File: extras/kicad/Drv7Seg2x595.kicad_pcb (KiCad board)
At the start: 2 copper layers, 67.4 x 50.8 mm, 33 parts, among them IC1 74HC595, IC2 74HC595, J1 INTERFACE, J2 PWR_LED_JMP, Q1 MMBT3904, Q2 MMBT3904, Q3 MMBT3904, Q4 MMBT3904

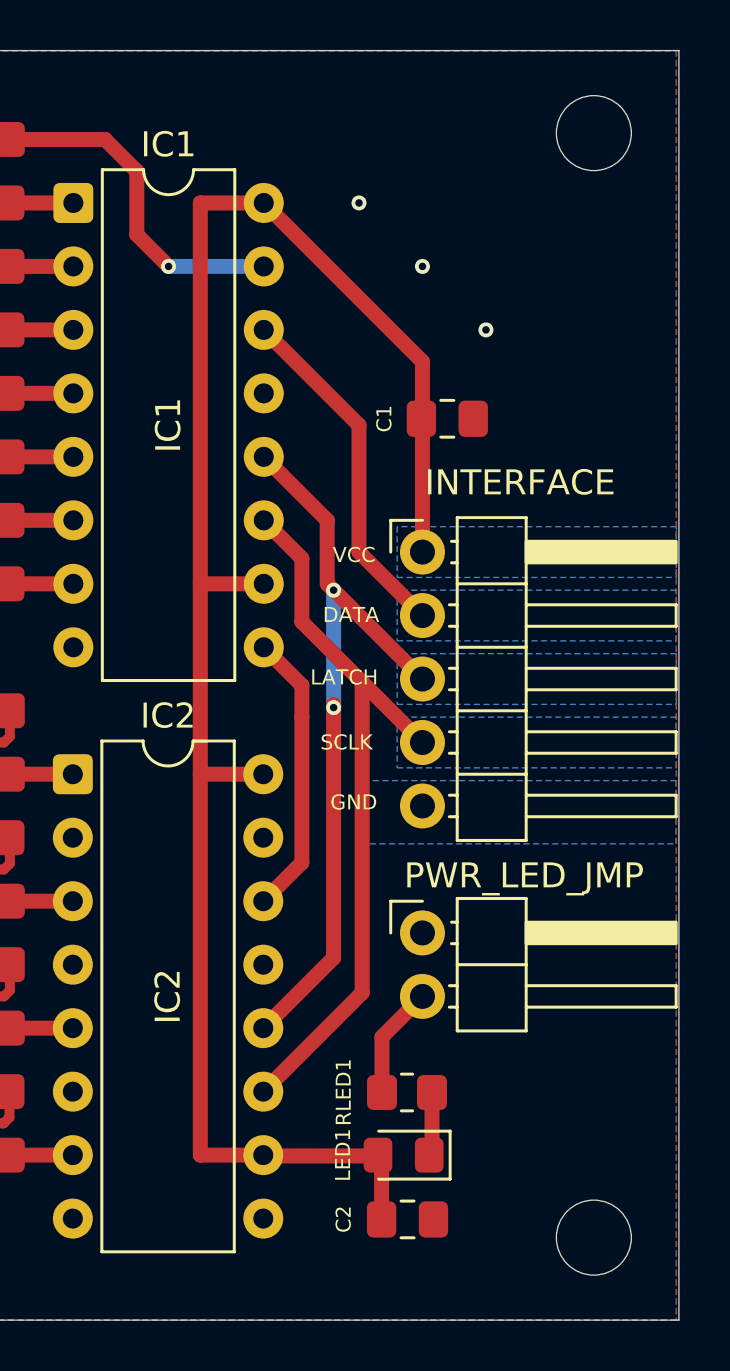
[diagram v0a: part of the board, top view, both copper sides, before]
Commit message: Move SMD caps, power indicator LED and its resistor behind the headers' line.
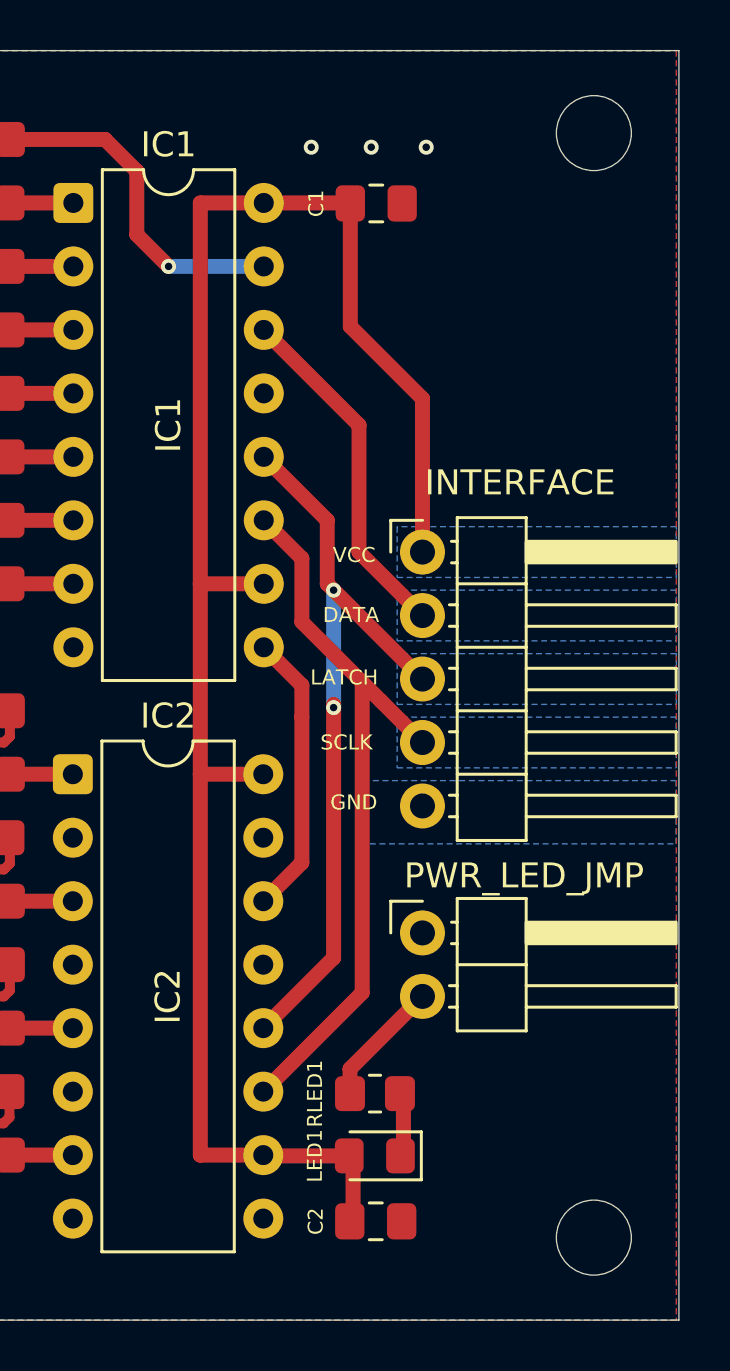
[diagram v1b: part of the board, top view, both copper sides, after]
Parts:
- moved C1 9.07 mm to (172.1, 73.7)
- moved RLED1 1.28 mm to (172.1, 109.3)
- moved C2 1.27 mm to (172.1, 114.4)
- moved D1 1.15 mm to (172.1, 111.8)
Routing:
- net VCC: track 72.1 -> 72.9 mm
- net Net-(J2-Pin_1): track 4.55 -> 5.11 mm
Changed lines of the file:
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@@
 	(footprint "Capacitor_SMD:C_0805_2012Metric_Pad1.18x1.45mm_HandSolder"
 		(layer "F.Cu")
-		(at 173.3925 114.334 180)
+		(at 172.12 114.41 180)
 		(descr "Capacitor SMD 0805 (2012 Metric), square (rectangular) end terminal, IPC-7351 nominal with elongated pad for handsoldering. (Body size source: IPC-SM-782 page 76, https://www.pcb-3d.com/wordpress/wp-content/uploads/ipc-sm-782a_amendment_1_and_2.pdf, https://docs.google.com/spreadsheets/d/1BsfQQcO9C6DZCsRaXUlFlo91Tg2WpOkGARC1WS5S8t0/edit?usp=sharing), generated with kicad-footprint-generator")
 		(tags "capacitor handsolder")
 		(property "Reference" "C2"
-			(at 2.5521 0.0086 90)
+			(at 2.4 0 90)
 			(layer "F.SilkS")
 			(effects
@@
 	(footprint "Resistor_SMD:R_0805_2012Metric_Pad1.20x1.40mm_HandSolder"
 		(layer "F.Cu")
-		(at 173.371 109.254)
+		(at 172.09 109.3)
 		(descr "Resistor SMD 0805 (2012 Metric), square (rectangular) end terminal, IPC-7351 nominal with elongated pad for handsoldering. (Body size source: IPC-SM-782 page 72, https://www.pcb-3d.com/wordpress/wp-content/uploads/ipc-sm-782a_amendment_1_and_2.pdf), generated with kicad-footprint-generator")
 		(tags "resistor handsolder")
 		(property "Reference" "RLED1"
-			(at -2.5306 -0.0086 90)
+			(at -2.4 0 90)
 			(layer "F.SilkS")
 			(effects
@@
 	(footprint "LED_SMD:LED_0805_2012Metric_Pad1.15x1.40mm_HandSolder"
 		(layer "F.Cu")
-		(at 173.237 111.76 180)
+		(at 172.085 111.79 180)
 		(descr "LED SMD 0805 (2012 Metric), square (rectangular) end terminal, IPC-7351 nominal, (Body size source: https://docs.google.com/spreadsheets/d/1BsfQQcO9C6DZCsRaXUlFlo91Tg2WpOkGARC1WS5S8t0/edit?usp=sharing), generated with kicad-footprint-generator")
 		(tags "LED handsolder")
@@
 		)
 		(property "Value" "LED1"
-			(at 2.422 0 90)
+			(at 2.4 0 90)
 			(layer "F.SilkS")
 			(effects
@@
 	(footprint "Capacitor_SMD:C_0805_2012Metric_Pad1.18x1.45mm_HandSolder"
 		(layer "F.Cu")
-		(at 174.9845 82.296)
+		(at 172.14 73.68)
 		(descr "Capacitor SMD 0805 (2012 Metric), square (rectangular) end terminal, IPC-7351 nominal with elongated pad for handsoldering. (Body size source: IPC-SM-782 page 76, https://www.pcb-3d.com/wordpress/wp-content/uploads/ipc-sm-782a_amendment_1_and_2.pdf, https://docs.google.com/spreadsheets/d/1BsfQQcO9C6DZCsRaXUlFlo91Tg2WpOkGARC1WS5S8t0/edit?usp=sharing), generated with kicad-footprint-generator")
 		(tags "capacitor handsolder")
 		(property "Reference" "C1"
-			(at -2.5185 0 90)
+			(at -2.4 0 90)
 			(layer "F.SilkS")
 			(effects
@@
 	)
 	(segment
-		(start 167.654 111.794)
-		(end 167.62 111.76)
+		(start 167.64 73.66)
+		(end 171.0825 73.66)
 		(width 0.6)
 		(layer "F.Cu")
@@
 	)
 	(segment
-		(start 172.355 111.794)
-		(end 172.355 114.334)
+		(start 167.654 111.794)
+		(end 167.62 111.76)
 		(width 0.6)
 		(layer "F.Cu")
@@
 	)
 	(segment
-		(start 173.99 87.63)
-		(end 173.99 80.01)
+		(start 171.213 111.824)
+		(end 171.213 114.364)
 		(width 0.6)
 		(layer "F.Cu")
@@
 	)
 	(segment
-		(start 165.1 88.9)
-		(end 165.1 73.66)
+		(start 171.0825 73.66)
+		(end 171.1025 73.68)
 		(width 0.6)
 		(layer "F.Cu")
@@
 	)
 	(segment
-		(start 172.355 111.794)
-		(end 167.654 111.794)
+		(start 165.1 88.9)
+		(end 165.1 73.66)
 		(width 0.6)
 		(layer "F.Cu")
@@
 	)
 	(segment
-		(start 165.1 73.66)
-		(end 167.64 73.66)
+		(start 171.1025 78.6025)
+		(end 173.99 81.49)
 		(width 0.6)
 		(layer "F.Cu")
@@
 	)
 	(segment
-		(start 173.99 80.01)
+		(start 165.1 73.66)
 		(end 167.64 73.66)
 		(width 0.6)
@@
 	)
 	(segment
+		(start 173.947 87.587)
+		(end 173.99 87.63)
+		(width 0.6)
+		(layer "F.Cu")
+		(net 9)
+	)
+	(segment
 		(start 165.1 96.52)
 		(end 165.1 111.76)
@@
 	)
 	(segment
+		(start 171.06 111.79)
+		(end 167.65 111.79)
+		(width 0.6)
+		(layer "F.Cu")
+		(net 9)
+	)
+	(segment
+		(start 171.1025 73.68)
+		(end 171.1025 78.6025)
+		(width 0.6)
+		(layer "F.Cu")
+		(net 9)
+	)
+	(segment
 		(start 167.64 88.9)
 		(end 165.1 88.9)
@@
 		(net 9)
 	)
+	(segment
+		(start 173.99 81.49)
+		(end 173.99 87.63)
+		(width 0.6)
+		(layer "F.Cu")
+		(net 9)
+	)
+	(segment
+		(start 167.65 111.79)
+		(end 167.62 111.76)
+		(width 0.2)
+		(layer "F.Cu")
+		(net 9)
+	)
 	(via
 		(at 153.67 103.886)
@@
 	)
 	(via
-		(at 148.59 72.39)
+		(at 174.14 71.43)
 		(size 0.6)
 		(drill 0.3)
@@
 	)
 	(via
-		(at 173.99 76.2)
+		(at 148.59 72.39)
 		(size 0.6)
 		(drill 0.3)
@@
 	)
 	(via
-		(at 171.45 73.66)
+		(at 171.94 71.43)
 		(size 0.6)
 		(drill 0.3)
@@
 	)
 	(via
-		(at 176.53 78.74)
+		(at 156.337 114.3)
 		(size 0.6)
 		(drill 0.3)
@@
 	)
 	(via
-		(at 156.337 114.3)
+		(at 148.59 74.93)
 		(size 0.6)
 		(drill 0.3)
@@
 	)
 	(via
-		(at 148.59 74.93)
+		(at 169.54 71.43)
 		(size 0.6)
 		(drill 0.3)
@@
 	)
 	(segment
-		(start 174.371 111.76)
-		(end 174.405 111.794)
+		(start 173.229 111.79)
+		(end 173.263 111.824)
 		(width 0.6)
 		(layer "F.Cu")
@@
 	)
 	(segment
-		(start 174.371 109.254)
-		(end 174.371 111.76)
+		(start 173.229 109.284)
+		(end 173.229 111.79)
 		(width 0.6)
 		(layer "F.Cu")
@@
 	)
 	(segment
-		(start 172.371 109.254)
-		(end 172.355 109.254)
+		(start 171.09 108.31)
+		(end 171.09 109.3)
 		(width 0.6)
 		(layer "F.Cu")
@@
 	)
 	(segment
-		(start 172.371 109.254)
-		(end 172.371 107.029)
+		(start 173.99 105.41)
+		(end 171.09 108.31)
 		(width 0.6)
 		(layer "F.Cu")
@@
 		(end 173.99 105.41)
 		(width 0.6)
-		(layer "F.Cu")
-		(net 41)
-	)
-	(segment
-		(start 172.371 107.029)
-		(end 173.99 105.41)
-		(width 0.6)

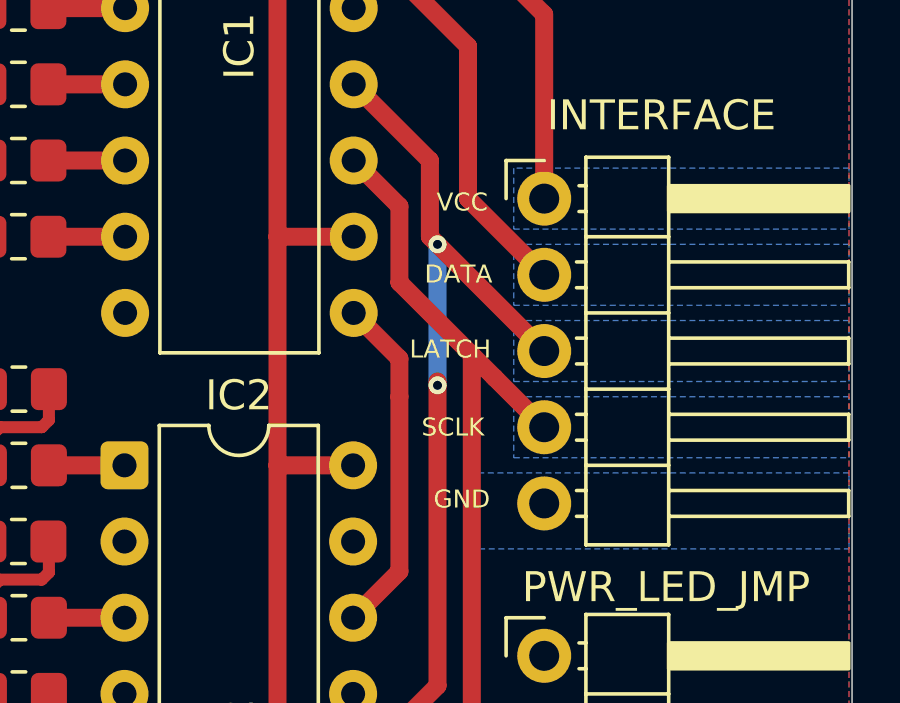
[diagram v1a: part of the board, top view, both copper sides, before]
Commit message: Restyle interface header labels + move mounting holes symbols on schematic a bit.
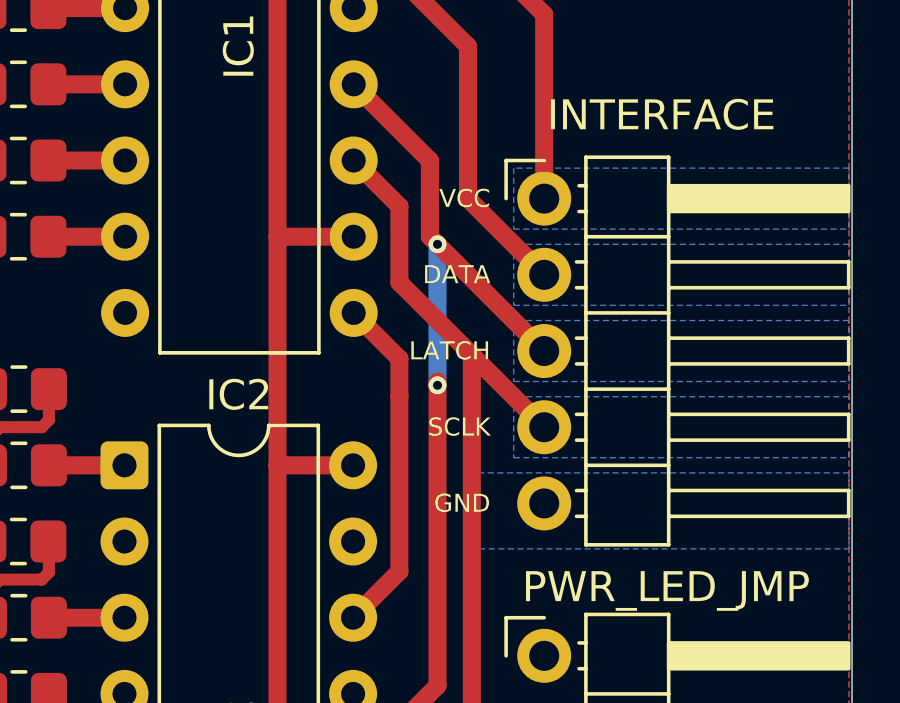
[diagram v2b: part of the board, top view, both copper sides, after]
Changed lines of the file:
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@@
 	)
 	(gr_text "LATCH"
-		(at 169.5 93 0)
-		(layer "F.SilkS")
+		(at 172.2 92.71 0)
+		(layer "F.SilkS" knockout)
 		(effects
 			(font
@@
 				(thickness 0.15)
 			)
-			(justify left bottom)
+			(justify right)
 		)
 	)
 	(gr_text "VCC"
-		(at 170.4 88.1 0)
-		(layer "F.SilkS")
+		(at 172.2 87.63 0)
+		(layer "F.SilkS" knockout)
 		(effects
 			(font
@@
 				(thickness 0.15)
 			)
-			(justify left bottom)
+			(justify right)
 		)
 	)
 	(gr_text "DATA"
-		(at 170 90.5 0)
-		(layer "F.SilkS")
+		(at 172.2 90.17 0)
+		(layer "F.SilkS" knockout)
 		(effects
 			(font
@@
 				(thickness 0.15)
 			)
-			(justify left bottom)
+			(justify right)
 		)
 	)
 	(gr_text "GND\n"
-		(at 170.3 98 0)
-		(layer "F.SilkS")
+		(at 172.2 97.79 0)
+		(layer "F.SilkS" knockout)
 		(effects
 			(font
@@
 				(thickness 0.15)
 			)
-			(justify left bottom)
+			(justify right)
 		)
 	)
 	(gr_text "SCLK"
-		(at 169.9 95.6 0)
-		(layer "F.SilkS")
+		(at 172.2 95.25 0)
+		(layer "F.SilkS" knockout)
 		(effects
 			(font
@@
 				(thickness 0.15)
 			)
-			(justify left bottom)
+			(justify right)
 		)
 	)

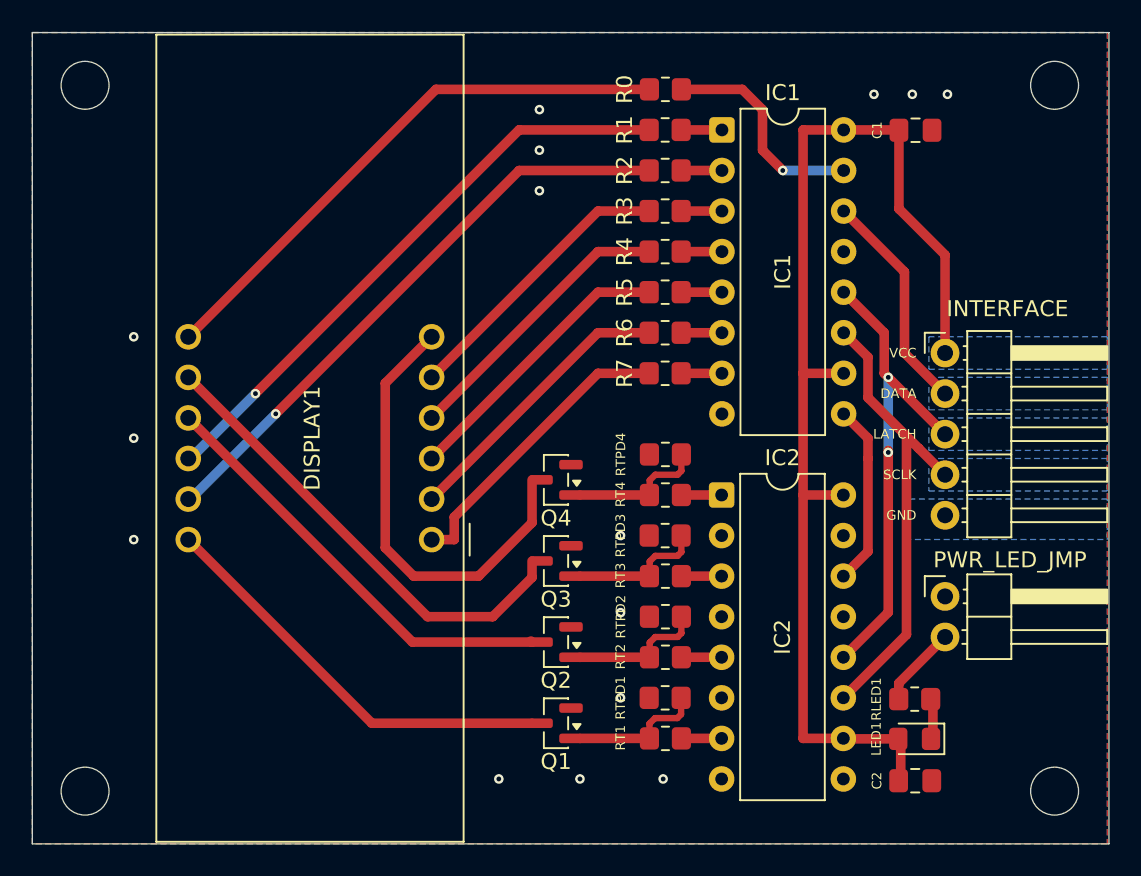
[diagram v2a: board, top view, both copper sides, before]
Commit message: Make steps towards more compact PCB.
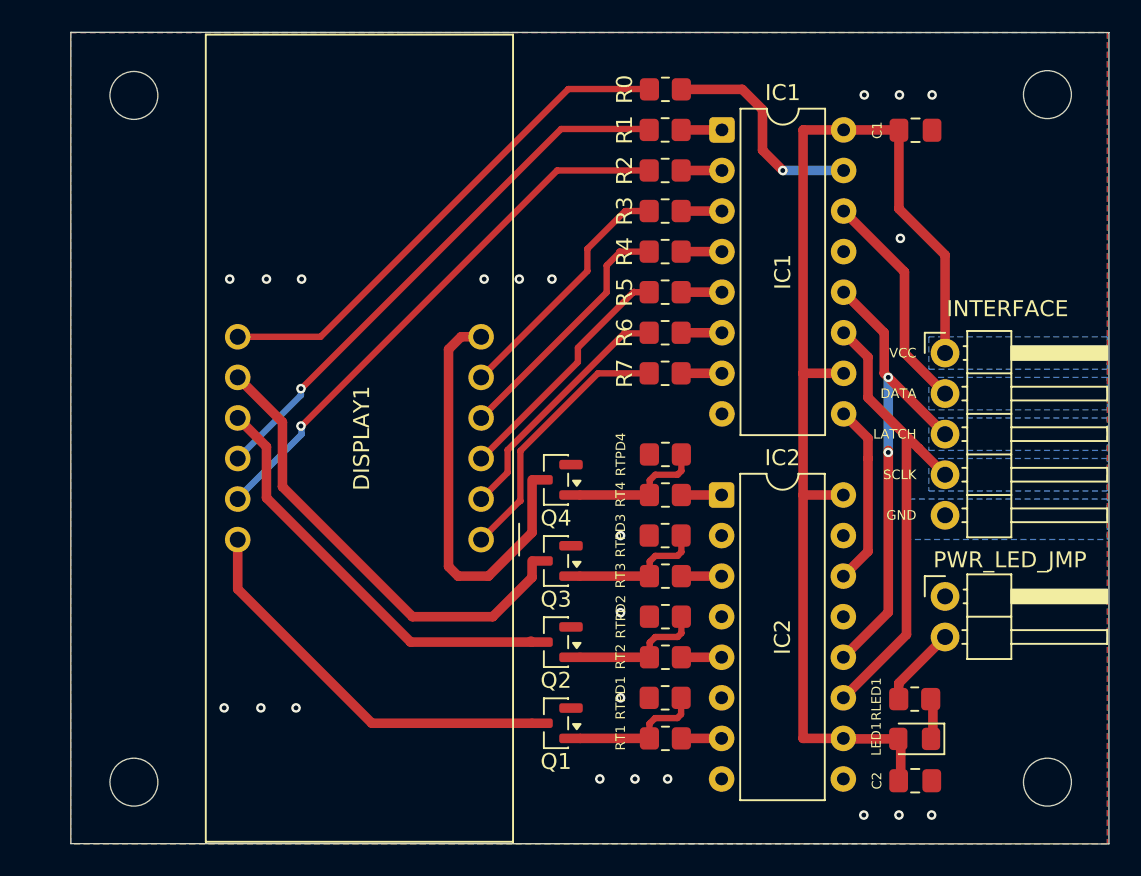
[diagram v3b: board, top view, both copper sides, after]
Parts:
- moved Hole4 74.4 mm to (180.4, 114.5)
- moved Hole1 57.7 mm to (123.2, 71.5)
- moved Hole2 43.6 mm to (180.4, 71.5)
- moved Hole3 3.11 mm to (123.2, 114.5)
- moved DISPLAY1 3.10 mm to (144.9, 99.3)
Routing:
- net Net-(DISPLAY1-B): track 35.3 -> 32.2 mm
- net Net-(DISPLAY1-A): track 37.4 -> 34.6 mm
- net Net-(DISPLAY1-DP): track 18.0 -> 15.4 mm
- net Net-(DISPLAY1-D4): track 28.4 -> 25.9 mm
- net Net-(DISPLAY1-F): track 37.4 -> 35.0 mm
- net Net-(DISPLAY1-G): track 17.9 -> 15.7 mm
- net Net-(DISPLAY1-D): track 17.9 -> 15.7 mm
- net Net-(DISPLAY1-C): track 17.9 -> 15.9 mm
- net Net-(DISPLAY1-E): track 18.8 -> 17.0 mm
- net Net-(DISPLAY1-D1): track 26.3 -> 25.0 mm
- net Net-(DISPLAY1-D2): track 27.4 -> 26.6 mm
- net Net-(DISPLAY1-D3): track 29.8 -> 29.1 mm
- net GND: vias 15 -> 22
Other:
- board size 67.4 x 50.8 mm -> 65 x 50.8 mm

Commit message: Make more steps towards more compact PCB, but keep components on one side yet.
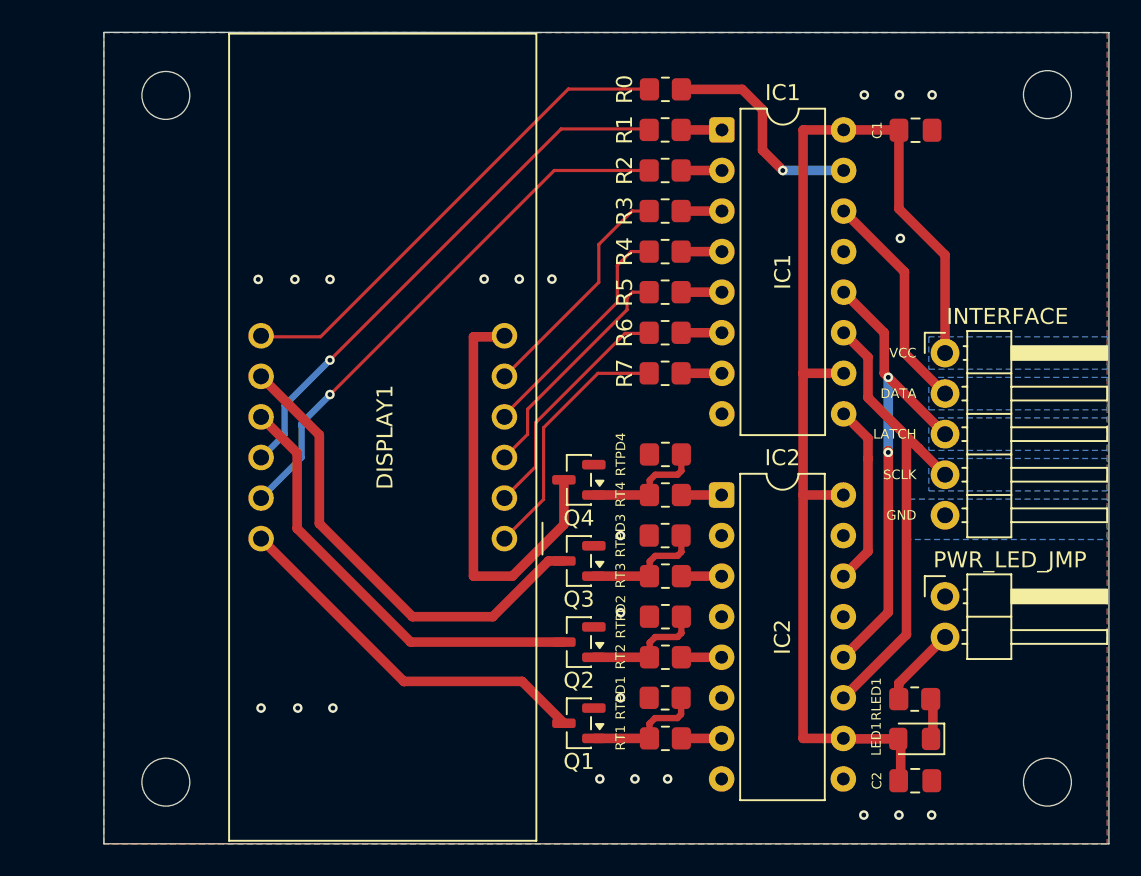
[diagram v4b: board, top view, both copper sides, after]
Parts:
- moved Hole1 2.00 mm to (125.2, 71.5)
- moved Hole3 2.00 mm to (125.2, 114.5)
- moved DISPLAY1 1.46 mm to (146.4, 99.2)
- moved Q1 1.43 mm to (151.1, 110.8)
- moved Q2 1.43 mm to (151.1, 105.7)
- moved Q3 1.43 mm to (151.1, 100.7)
- moved Q4 1.43 mm to (151.1, 95.6)
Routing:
- net Net-(DISPLAY1-D2): track 26.6 -> 28.0 mm
- net Net-(DISPLAY1-B): track 32.2 -> 30.8 mm
- net Net-(DISPLAY1-D1): track 25.0 -> 23.8 mm
- net Net-(DISPLAY1-C): track 15.9 -> 14.8 mm
- net Net-(DISPLAY1-E): track 17.0 -> 16.1 mm
- net Net-(DISPLAY1-G): track 15.7 -> 14.7 mm
- net Net-(DISPLAY1-D4): track 25.9 -> 26.8 mm
- net Net-(Q3-B): track 8.53 -> 7.66 mm
- net Net-(Q2-B): track 8.53 -> 7.66 mm
- net Net-(Q1-B): track 8.53 -> 7.66 mm
- net Net-(Q4-B): track 8.53 -> 7.66 mm
- net Net-(DISPLAY1-D3): track 29.1 -> 29.9 mm
- net Net-(DISPLAY1-D): track 15.7 -> 14.9 mm
- net Net-(DISPLAY1-F): track 35.0 -> 34.4 mm
- net Net-(DISPLAY1-DP): track 15.4 -> 14.8 mm
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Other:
- board size 65 x 50.8 mm -> 62.9 x 50.8 mm
